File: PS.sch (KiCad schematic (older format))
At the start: 2 parts, among them P1 5V, P2 12V

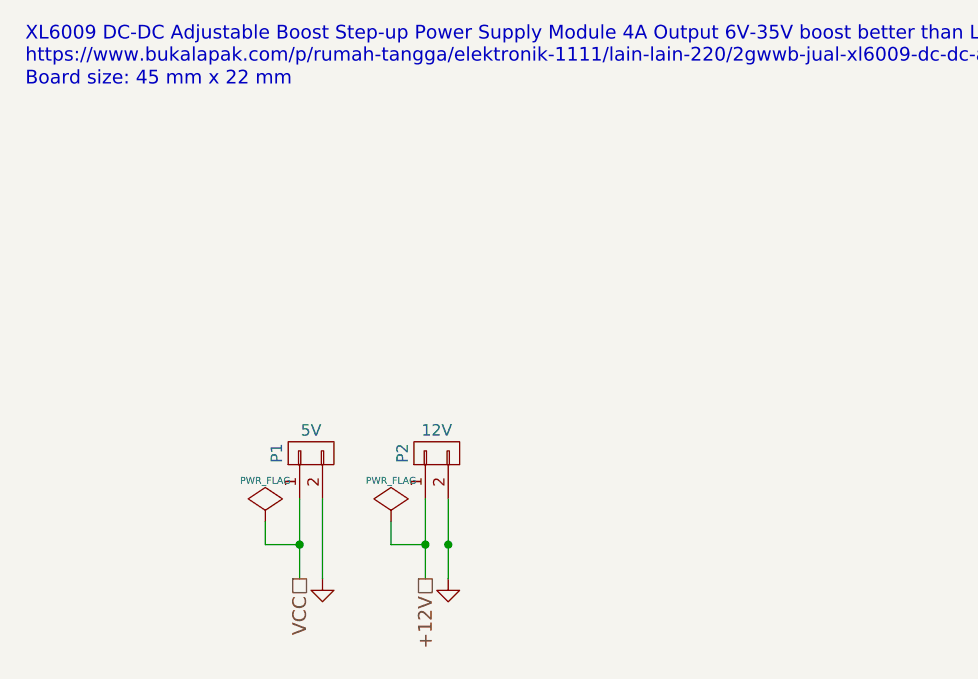
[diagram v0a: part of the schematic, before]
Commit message: Changes to be committed: 	new file:   78LXXSOT89.pdf 	modified:   Control.sch 	modified:   Debugger.sch 	modified:   MotorDriver.sch 	modified:   PS.sch 	modified:   Sensor.sch 	new file:   XL6009-Schematic-Diagram.pdf 	modified:   main-cache.lib 	new file:   main.cmp 	new file:   main.kicad_pcb 	new file:   main.net 	modified:   main.pro 	modified:   main.sch
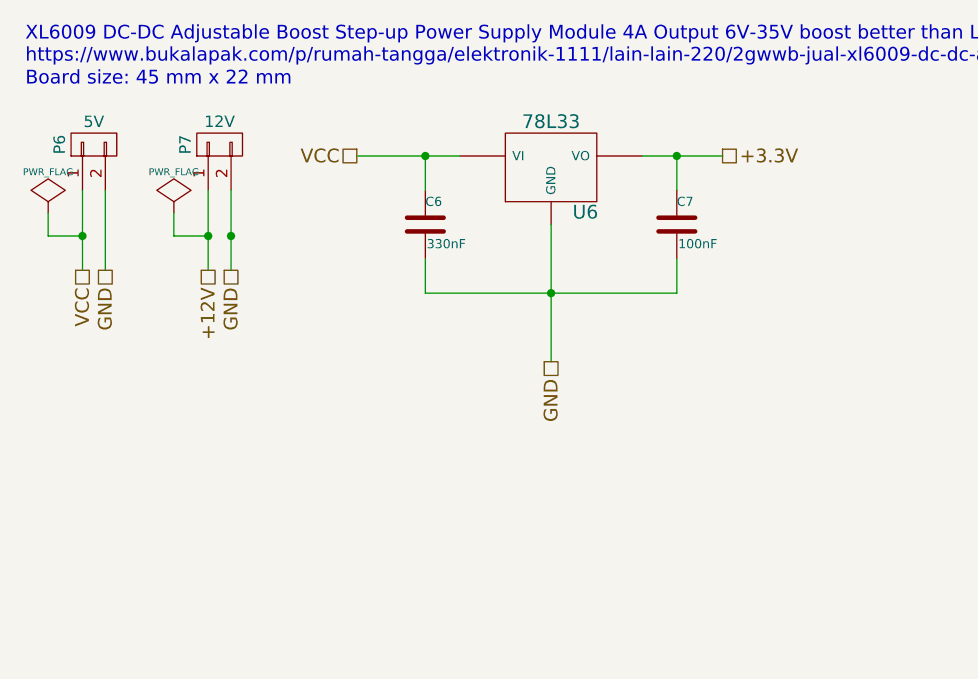
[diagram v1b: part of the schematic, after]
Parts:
- added C6: 330nF, Capacitors_SMD:C_0805_HandSoldering, symbol C
- added C7: 100nF, Capacitors_SMD:C_0805_HandSoldering, symbol C
- added U6: 78L33, Discret:LM78LXX, symbol 78L05
- P6: renamed from P1; footprint (none) -> Socket_Strips:Socket_Strip_Straight_1x02
- P7: renamed from P2; footprint (none) -> Socket_Strips:Socket_Strip_Straight_1x02
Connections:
- net GND: now also C6.2, C7.2, U6.GND
- net VCC: now also C6.1, U6.VI
- new net +3.3V: C7.1, U6.VO
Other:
- moved on the sheet: P6, P7
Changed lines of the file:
@@
 EESchema Schematic File Version 2
+LIBS:main-rescue
 LIBS:power
 LIBS:device
@@
 LIBS:contrib
 LIBS:main-cache
+LIBS:tcrt5000
 EELAYER 25 0
 EELAYER END
 $Descr A4 11693 8268
 encoding utf-8
-Sheet 2 6
+Sheet 5 6
 Title ""
 Date ""
@@
 70 CE 10 4A 52 8A C6 CE 99 24 21 D4 FD 7E 5F 16 8B 0E CD 34 4D C6 AE F4 63 6B ED 30 8E 7D DF 03
 FE CD 99 20 1E EE F7 FB 97 97 17 C6 98 77 1E C0 C7 36 ED 7D B9 5C A0 E9 2A 8A 45 F9 FF 03 C7 AE
-FC 30 55 0D 68 40 00 00 00 00 49 45 4E 44 AE 42 60 82 00
+FC 30 55 0D 68 40 00 00 00 00 49 45 4E 44 AE 42 60 82 09
 EndData
 $EndBitmap
@@
 Board size: 45 mm x 22 mm
 $Comp
-L CONN_01X02 P1
+L CONN_01X02 P6
 U 1 1 558D360C
-P 1850 4050
-F 0 "P1" H 1850 4200 50  0000 C CNN
-F 1 "5V" V 1950 4050 50  0000 C CNN
-F 2 "" H 1850 4050 60  0000 C CNN
-F 3 "" H 1850 4050 60  0000 C CNN
-	1    1850 4050
+P 900 2700
+F 0 "P6" H 900 2850 50  0000 C CNN
+F 1 "5V" V 1000 2700 50  0000 C CNN
+F 2 "Socket_Strips:Socket_Strip_Straight_1x02" H 900 2700 60  0001 C CNN
+F 3 "" H 900 2700 60  0000 C CNN
+	1    900  2700
 	0    -1   -1   0
 $EndComp
 $Comp
-L CONN_01X02 P2
+L CONN_01X02 P7
 U 1 1 558D36AA
-P 2400 4050
-F 0 "P2" H 2400 4200 50  0000 C CNN
-F 1 "12V" V 2500 4050 50  0000 C CNN
-F 2 "" H 2400 4050 60  0000 C CNN
-F 3 "" H 2400 4050 60  0000 C CNN
-	1    2400 4050
+P 1450 2700
+F 0 "P7" H 1450 2850 50  0000 C CNN
+F 1 "12V" V 1550 2700 50  0000 C CNN
+F 2 "Socket_Strips:Socket_Strip_Straight_1x02" H 1450 2700 60  0001 C CNN
+F 3 "" H 1450 2700 60  0000 C CNN
+	1    1450 2700
 	0    -1   -1   0
 $EndComp
+Wire Wire Line
+	1500 2900 1500 3250
+Wire Wire Line
+	950  2900 950  3250
+Text HLabel 850  3250 3    60   UnSpc ~ 0
+VCC
+Text HLabel 1400 3250 3    60   UnSpc ~ 0
++12V
+Wire Wire Line
+	1400 2900 1400 3250
+Wire Wire Line
+	850  2900 850  3250
 $Comp
-L GND #PWR02
-U 1 1 558D3B67
-P 1900 4600
-F 0 "#PWR02" H 1900 4600 30  0001 C CNN
-F 1 "GND" H 1900 4530 30  0001 C CNN
-F 2 "" H 1900 4600 60  0000 C CNN
-F 3 "" H 1900 4600 60  0000 C CNN
-	1    1900 4600
+L PWR_FLAG #FLG011
+U 1 1 558D3DFD
+P 1250 3000
+F 0 "#FLG011" H 1250 3095 30  0001 C CNN
+F 1 "PWR_FLAG" H 1250 3180 30  0000 C CNN
+F 2 "" H 1250 3000 60  0000 C CNN
+F 3 "" H 1250 3000 60  0000 C CNN
+	1    1250 3000
 	1    0    0    -1
 $EndComp
 $Comp
-L GND #PWR03
-U 1 1 558D3B7B
-P 2450 4600
-F 0 "#PWR03" H 2450 4600 30  0001 C CNN
-F 1 "GND" H 2450 4530 30  0001 C CNN
-F 2 "" H 2450 4600 60  0000 C CNN
-F 3 "" H 2450 4600 60  0000 C CNN
-	1    2450 4600
+L PWR_FLAG #FLG012
+U 1 1 558D3E11
+P 700 3000
+F 0 "#FLG012" H 700 3095 30  0001 C CNN
+F 1 "PWR_FLAG" H 700 3180 30  0000 C CNN
+F 2 "" H 700 3000 60  0000 C CNN
+F 3 "" H 700 3000 60  0000 C CNN
+	1    700  3000
 	1    0    0    -1
 $EndComp
 Wire Wire Line
-	2450 4250 2450 4600
+	700  3000 700  3100
+Wire Wire Line
+	700  3100 850  3100
+Connection ~ 850  3100
 Wire Wire Line
-	1900 4250 1900 4600
-Text HLabel 1800 4600 3    60   UnSpc ~ 0
+	1250 3000 1250 3100
+Wire Wire Line
+	1250 3100 1400 3100
+Connection ~ 1400 3100
+Connection ~ 1500 3100
+$Comp
+L 78L05 U6
+U 1 1 558DC42E
+P 2900 2800
+F 0 "U6" H 3050 2604 60  0000 C CNN
+F 1 "78L33" H 2900 3000 60  0000 C CNN
+F 2 "Discret:LM78LXX" H 2900 2800 60  0001 C CNN
+F 3 "" H 2900 2800 60  0000 C CNN
+	1    2900 2800
+	1    0    0    -1
+$EndComp
+Text HLabel 2050 2750 0    60   UnSpc ~ 0
 VCC
-Text HLabel 2350 4600 3    60   UnSpc ~ 0
-+12V
+Text HLabel 1500 3250 3    60   UnSpc ~ 0
+GND
+Text HLabel 950  3250 3    60   UnSpc ~ 0
+GND
+Text HLabel 2900 3650 3    60   UnSpc ~ 0
+GND
+Text HLabel 3650 2750 2    60   UnSpc ~ 0
++3.3V
 Wire Wire Line
-	2350 4250 2350 4600
+	3300 2750 3650 2750
 Wire Wire Line
-	1800 4250 1800 4600
+	2900 3050 2900 3650
+Wire Wire Line
+	2050 2750 2500 2750
 $Comp
-L PWR_FLAG #FLG04
-U 1 1 558D3DFD
-P 2200 4350
-F 0 "#FLG04" H 2200 4445 30  0001 C CNN
-F 1 "PWR_FLAG" H 2200 4530 30  0000 C CNN
-F 2 "" H 2200 4350 60  0000 C CNN
-F 3 "" H 2200 4350 60  0000 C CNN
-	1    2200 4350
+L C C6
+U 1 1 558DCFD1
+P 2350 3050
+F 0 "C6" H 2350 3150 40  0000 L CNN
+F 1 "330nF" H 2356 2965 40  0000 L CNN
+F 2 "Capacitors_SMD:C_0805_HandSoldering" H 2388 2900 30  0001 C CNN
+F 3 "" H 2350 3050 60  0000 C CNN
+	1    2350 3050
 	1    0    0    -1
 $EndComp
 $Comp
-L PWR_FLAG #FLG05
-U 1 1 558D3E11
-P 1650 4350
-F 0 "#FLG05" H 1650 4445 30  0001 C CNN
-F 1 "PWR_FLAG" H 1650 4530 30  0000 C CNN
-F 2 "" H 1650 4350 60  0000 C CNN
-F 3 "" H 1650 4350 60  0000 C CNN
-	1    1650 4350
+L C C7
+U 1 1 558DD028
+P 3450 3050
+F 0 "C7" H 3450 3150 40  0000 L CNN
+F 1 "100nF" H 3456 2965 40  0000 L CNN
+F 2 "Capacitors_SMD:C_0805_HandSoldering" H 3488 2900 30  0001 C CNN
+F 3 "" H 3450 3050 60  0000 C CNN
+	1    3450 3050
 	1    0    0    -1
 $EndComp
 Wire Wire Line
-	1650 4350 1650 4450
+	3450 3200 3450 3350
+Wire Wire Line
+	3450 3350 2350 3350
+Connection ~ 2900 3350
 Wire Wire Line
-	1650 4450 1800 4450
-Connection ~ 1800 4450
+	2350 3350 2350 3200
 Wire Wire Line
-	2200 4350 2200 4450
+	2350 2750 2350 2900
+Connection ~ 2350 2750
 Wire Wire Line
-	2200 4450 2350 4450
-Connection ~ 2350 4450
-Connection ~ 2450 4450
+	3450 2750 3450 2900
+Connection ~ 3450 2750
 $EndSCHEMATC

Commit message: update
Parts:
- removed P7: 12V, Socket_Strips:Socket_Strip_Straight_1x02, symbol CONN_01X02
- removed U6: 78L33, Discret:LM78LXX, symbol 78L05
- added C8: 330nF, Capacitors_SMD:C_0805_HandSoldering, symbol C
- added C9: 100nF, Capacitors_SMD:C_0805_HandSoldering, symbol C
- added P8: 12V, Pin_Headers:Pin_Header_Straight_1x03, symbol CONN_01X03
- added U1: LM7805, Discret:LM78XX-TO92, symbol LM7805
- added U2: 78L33, Discret:LM78XX-TO92, symbol 78L05
- renumbered P6 to P7
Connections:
- net +12V: now also C6.1, P8.1 (P1), U1.VI
- net +3.3V: now also C9.1, U2.VO; no longer C7.1
- net GND: now also C8.2, C9.2, P8.2 (P2), U1.GND, U2.GND
- net VCC: now also C7.1, C8.1, U1.VO, U2.VI; no longer C6.1, P7.1 (P1)
- new net: P7.1 (P1), P8.3 (P3)
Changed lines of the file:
@@
 LIBS:memory
 LIBS:xilinx
-LIBS:special
 LIBS:microcontrollers
 LIBS:dsp
@@
 encoding utf-8
 Sheet 5 6
-Title ""
-Date ""
-Rev ""
+Title "KENZANIN LINEFOLLOWER"
+Date "2015-06-28"
+Rev "1.0"
 Comp ""
 Comment1 ""
@@
 70 CE 10 4A 52 8A C6 CE 99 24 21 D4 FD 7E 5F 16 8B 0E CD 34 4D C6 AE F4 63 6B ED 30 8E 7D DF 03
 FE CD 99 20 1E EE F7 FB 97 97 17 C6 98 77 1E C0 C7 36 ED 7D B9 5C A0 E9 2A 8A 45 F9 FF 03 C7 AE
-FC 30 55 0D 68 40 00 00 00 00 49 45 4E 44 AE 42 60 82 09
+FC 30 55 0D 68 40 00 00 00 00 49 45 4E 44 AE 42 60 82 E7
 EndData
 $EndBitmap
@@
 Board size: 45 mm x 22 mm
 $Comp
-L CONN_01X02 P6
+L CONN_01X02 P7
 U 1 1 558D360C
 P 900 2700
-F 0 "P6" H 900 2850 50  0000 C CNN
+F 0 "P7" H 900 2850 50  0000 C CNN
 F 1 "5V" V 1000 2700 50  0000 C CNN
 F 2 "Socket_Strips:Socket_Strip_Straight_1x02" H 900 2700 60  0001 C CNN
@@
 	0    -1   -1   0
 $EndComp
-$Comp
-L CONN_01X02 P7
-U 1 1 558D36AA
-P 1450 2700
-F 0 "P7" H 1450 2850 50  0000 C CNN
-F 1 "12V" V 1550 2700 50  0000 C CNN
-F 2 "Socket_Strips:Socket_Strip_Straight_1x02" H 1450 2700 60  0001 C CNN
-F 3 "" H 1450 2700 60  0000 C CNN
-	1    1450 2700
-	0    -1   -1   0
-$EndComp
 Wire Wire Line
 	1500 2900 1500 3250
 Wire Wire Line
 	950  2900 950  3250
-Text HLabel 850  3250 3    60   UnSpc ~ 0
-VCC
 Text HLabel 1400 3250 3    60   UnSpc ~ 0
 +12V
 Wire Wire Line
 	1400 2900 1400 3250
-Wire Wire Line
-	850  2900 850  3250
 $Comp
 L PWR_FLAG #FLG011
@@
 	1    0    0    -1
 $EndComp
-$Comp
-L PWR_FLAG #FLG012
-U 1 1 558D3E11
-P 700 3000
-F 0 "#FLG012" H 700 3095 30  0001 C CNN
-F 1 "PWR_FLAG" H 700 3180 30  0000 C CNN
-F 2 "" H 700 3000 60  0000 C CNN
-F 3 "" H 700 3000 60  0000 C CNN
-	1    700  3000
-	1    0    0    -1
-$EndComp
-Wire Wire Line
-	700  3000 700  3100
-Wire Wire Line
-	700  3100 850  3100
-Connection ~ 850  3100
 Wire Wire Line
 	1250 3000 1250 3100
@@
 Connection ~ 1400 3100
 Connection ~ 1500 3100
-$Comp
-L 78L05 U6
-U 1 1 558DC42E
-P 2900 2800
-F 0 "U6" H 3050 2604 60  0000 C CNN
-F 1 "78L33" H 2900 3000 60  0000 C CNN
-F 2 "Discret:LM78LXX" H 2900 2800 60  0001 C CNN
-F 3 "" H 2900 2800 60  0000 C CNN
-	1    2900 2800
-	1    0    0    -1
-$EndComp
-Text HLabel 2050 2750 0    60   UnSpc ~ 0
-VCC
 Text HLabel 1500 3250 3    60   UnSpc ~ 0
 GND
@@
 Text HLabel 2900 3650 3    60   UnSpc ~ 0
 GND
-Text HLabel 3650 2750 2    60   UnSpc ~ 0
-+3.3V
 Wire Wire Line
 	3300 2750 3650 2750
@@
 	3450 2750 3450 2900
 Connection ~ 3450 2750
+$Comp
+L 78L05 U2
+U 1 1 55901EC1
+P 5400 2800
+F 0 "U2" H 5550 2604 60  0000 C CNN
+F 1 "78L33" H 5400 3000 60  0000 C CNN
+F 2 "Discret:LM78XX-TO92" H 5400 2800 60  0001 C CNN
+F 3 "" H 5400 2800 60  0000 C CNN
+	1    5400 2800
+	1    0    0    -1
+$EndComp
+Text HLabel 5400 3650 3    60   UnSpc ~ 0
+GND
+Text HLabel 6150 2750 2    60   UnSpc ~ 0
++3.3V
+Wire Wire Line
+	5800 2750 6150 2750
+Wire Wire Line
+	5400 3050 5400 3650
+Wire Wire Line
+	4550 2750 5000 2750
+$Comp
+L C C8
+U 1 1 55901ECD
+P 4850 3050
+F 0 "C8" H 4850 3150 40  0000 L CNN
+F 1 "330nF" H 4856 2965 40  0000 L CNN
+F 2 "Capacitors_SMD:C_0805_HandSoldering" H 4888 2900 30  0001 C CNN
+F 3 "" H 4850 3050 60  0000 C CNN
+	1    4850 3050
+	1    0    0    -1
+$EndComp
+$Comp
+L C C9
+U 1 1 55901ED3
+P 5950 3050
+F 0 "C9" H 5950 3150 40  0000 L CNN
+F 1 "100nF" H 5956 2965 40  0000 L CNN
+F 2 "Capacitors_SMD:C_0805_HandSoldering" H 5988 2900 30  0001 C CNN
+F 3 "" H 5950 3050 60  0000 C CNN
+	1    5950 3050
+	1    0    0    -1
+$EndComp
+Wire Wire Line
+	5950 3200 5950 3350
+Wire Wire Line
+	5950 3350 4850 3350
+Connection ~ 5400 3350
+Wire Wire Line
+	4850 3350 4850 3200
+Wire Wire Line
+	4850 2750 4850 2900
+Connection ~ 4850 2750
+Wire Wire Line
+	5950 2750 5950 2900
+Connection ~ 5950 2750
+Text HLabel 2050 2750 0    60   UnSpc ~ 0
++12V
+Text HLabel 3650 2750 2    60   UnSpc ~ 0
+VCC
+Text HLabel 4550 2750 0    60   UnSpc ~ 0
+VCC
+$Comp
+L CONN_01X03 P8
+U 1 1 55902DC8
+P 1500 2700
+F 0 "P8" H 1500 2900 50  0000 C CNN
+F 1 "12V" V 1600 2700 50  0000 C CNN
+F 2 "Pin_Headers:Pin_Header_Straight_1x03" H 1500 2700 60  0001 C CNN
+F 3 "" H 1500 2700 60  0000 C CNN
+	1    1500 2700
+	0    -1   -1   0
+$EndComp
+Wire Wire Line
+	850  2900 850  3200
+Wire Wire Line
+	850  3200 1600 3200
+Wire Wire Line
+	1600 3200 1600 2900
+$Comp
+L LM7805 U1
+U 1 1 55906F15
+P 2900 2800
+F 0 "U1" H 3050 2604 60  0000 C CNN
+F 1 "LM7805" H 2900 3000 60  0000 C CNN
+F 2 "Discret:LM78XX-TO92" H 2900 2800 60  0001 C CNN
+F 3 "" H 2900 2800 60  0000 C CNN
+	1    2900 2800
+	1    0    0    -1
+$EndComp
 $EndSCHEMATC
